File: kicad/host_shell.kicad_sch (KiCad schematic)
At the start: 242 parts, among them J1 FG PH-2AWT, J10 Memory Card Slot, J11 Conn_02x12_Odd_Even, J2 Conn_01x02, J3 Conn_01x02, J4 Conn_01x40, J5 Conn_02x10_Odd_Even, J6 Conn_01x03, J7 Conn_01x02, J8 PJ-316A-6A, J9 Conn_01x02, P1 TYPE-C16PIN, Q1 IRLML2246TRPBF, Q4 BSS138W, Q5 BSS84W, Q6 BSS138W, Q7 BSS138W, SW1 GT-TC018A-H0375-L1, SW10 Rubber, SW11 SKRPACE010_6, SW12 Rubber, SW13 Rubber, SW2 Rubber, SW3 Rubber, SW4 Rubber, SW5 Rubber, SW6 Rubber, SW7 Rubber, SW8 Rubber, SW9 Rubber, U1 MCP73831-2-OT, U10 LM4880MX/NOPB, U11 LM4890S, U12 SN74LVC1G3157DBVR, U13 SN74AHC541PWR, U14 TPS22919DCKR, U15 RV-3028-C7, U2 XC6194AA03ER-G, U3 TPS63802, U4 PCA9555PW, U5 W25Q32JVSSIQ, U6 APS6404L-3SQRx-SN, U7 RP2350B, U8 74LVC2G17GW, U9 LM4890S, Y1 ABM8-272-T3

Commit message: wip
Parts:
- removed C23: 100n, Capacitor_SMD:C_0402_1005Metric, symbol Device:C_Small
- removed JP2, JP3, JP4: SolderJumper_3_Bridged12, Jumper:SolderJumper-3_P1.3mm_Bridged12_RoundedPad1.0x1.5mm, symbol shpc_mechanical:SolderJumper_3_Bridged12
- J2, J3: footprint shpc_mechanical:SolderWirePad_1x02_SMD_150x50mil -> shpc_mechanical:SolderWirePad_1x02_SMD_2.5x1.5mm
- J7, J9: footprint shpc_mechanical:SolderWirePad_1x02_SMD_150x50mil -> shpc_mechanical:SolderWirePad_2x01_SMD_2.5x1.5mm
- SW10, SW12, SW13, SW2, SW3, SW4, SW5, SW6, SW7, SW8, SW9: footprint shpc_mechanical:Rubber_Contact -> Button_Switch_SMD:SW_SPST_PTS645Sx43SMTR92
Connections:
- net 3V3: now also U4.21 (A0)
- net GND: now also J10.10 (DET_A), U4.2 (A1), U4.3 (A2); no longer J10.9 (DET_B)
- net HSAUDIO_L: now also U8.3 (2A); no longer U8.1 (1A)
- net HSAUDIO_R: now also U8.1 (1A); no longer U8.3 (2A)
- net HSLCD_CSX: now also U7.27 (GPIO26); no longer U7.25 (GPIO24)
- net HSLCD_RDX: now also U7.25 (GPIO24); no longer U7.22 (GPIO22)
- net HSLCD_RSTX: now also U7.23 (GPIO23); no longer U7.21 (GPIO21)
- net HSLCD_WRX: now also U7.26 (GPIO25); no longer U7.23 (GPIO23)
- net HSTF_DETX: now also J10.9 (DET_B); no longer J10.10 (DET_A)
- net LCA0: no longer TP17.1
- net at R45.1: now also U7.21 (GPIO21); no longer U7.26 (GPIO25)
- net at R46.1: now also U7.22 (GPIO22); no longer U7.27 (GPIO26)
- net at U8.4 (2Y): now also R50.1; no longer R51.1
- net at U8.6 (1Y): now also R51.1; no longer R50.1
- net at U4.1 (~{INT}): now also TP17.1
- no-connect marks 17 -> 16
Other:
- moved on the sheet: C24, C25, C26, C27, C28, C29, C30, C31, C32, C33, R70

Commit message: wip
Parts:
- J11, J5: now not fitted
- SW10, SW12, SW13, SW2, SW3, SW4, SW5, SW6, SW7, SW8, SW9: value Rubber -> PTS645SL50SMTR92; now not fitted
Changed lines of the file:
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@@
 		(on_board yes)
 		(in_pos_files yes)
-		(dnp no)
+		(dnp yes)
 		(property "Reference" "SW8"
 			(at 341.122 24.638 0)
@@
 			)
 		)
-		(property "Value" "Rubber"
+		(property "Value" "PTS645SL50SMTR92"
 			(at 341.884 24.638 0)
 			(show_name no)
@@
 		(on_board yes)
 		(in_pos_files yes)
-		(dnp no)
+		(dnp yes)
 		(property "Reference" "SW10"
 			(at 341.122 28.702 0)
@@
 			)
 		)
-		(property "Value" "Rubber"
+		(property "Value" "PTS645SL50SMTR92"
 			(at 341.884 28.702 0)
 			(show_name no)
@@
 		(on_board yes)
 		(in_pos_files yes)
-		(dnp no)
+		(dnp yes)
 		(property "Reference" "SW2"
 			(at 314.452 22.606 0)
@@
 			)
 		)
-		(property "Value" "Rubber"
+		(property "Value" "PTS645SL50SMTR92"
 			(at 315.214 22.606 0)
 			(show_name no)
@@
 		(on_board yes)
 		(in_pos_files yes)
-		(dnp no)
+		(dnp yes)
 		(property "Reference" "SW3"
 			(at 314.452 24.638 0)
@@
 			)
 		)
-		(property "Value" "Rubber"
+		(property "Value" "PTS645SL50SMTR92"
 			(at 315.214 24.638 0)
 			(show_name no)
@@
 		(on_board yes)
 		(in_pos_files yes)
-		(dnp no)
+		(dnp yes)
 		(property "Reference" "SW13"
 			(at 341.376 57.15 0)
@@
 			)
 		)
-		(property "Value" "Rubber"
+		(property "Value" "PTS645SL50SMTR92"
 			(at 342.138 57.15 0)
 			(show_name no)
@@
 		(on_board yes)
 		(in_pos_files yes)
-		(dnp no)
+		(dnp yes)
 		(property "Reference" "SW12"
 			(at 341.376 55.118 0)
@@
 			)
 		)
-		(property "Value" "Rubber"
+		(property "Value" "PTS645SL50SMTR92"
 			(at 342.138 55.118 0)
 			(show_name no)
@@
 		(on_board yes)
 		(in_pos_files yes)
-		(dnp no)
+		(dnp yes)
 		(property "Reference" "SW9"
 			(at 341.122 26.67 0)
@@
 			)
 		)
-		(property "Value" "Rubber"
+		(property "Value" "PTS645SL50SMTR92"
 			(at 341.884 26.67 0)
 			(show_name no)
@@
 		(on_board yes)
 		(in_pos_files yes)
-		(dnp no)
+		(dnp yes)
 		(property "Reference" "SW5"
 			(at 314.452 28.702 0)
@@
 			)
 		)
-		(property "Value" "Rubber"
+		(property "Value" "PTS645SL50SMTR92"
 			(at 315.214 28.702 0)
 			(show_name no)
@@
 		(on_board yes)
 		(in_pos_files yes)
-		(dnp no)
+		(dnp yes)
 		(property "Reference" "SW7"
 			(at 341.122 22.606 0)
@@
 			)
 		)
-		(property "Value" "Rubber"
+		(property "Value" "PTS645SL50SMTR92"
 			(at 341.884 22.606 0)
 			(show_name no)
@@
 		(on_board yes)
 		(in_pos_files yes)
-		(dnp no)
+		(dnp yes)
 		(property "Reference" "SW6"
-			(at 331.216 81.788 90)
+			(at 329.438 82.804 90)
 			(show_name no)
 			(do_not_autoplace no)
@@
 					(size 1.27 1.27)
 				)
-				(justify left)
+				(justify right)
 			)
 		)
-		(property "Value" "Rubber"
-			(at 331.216 83.82 90)
+		(property "Value" "PTS645SL50SMTR92"
+			(at 329.438 84.836 90)
 			(show_name no)
 			(do_not_autoplace no)
@@
 					(size 1.27 1.27)
 				)
-				(justify left)
+				(justify right)
 			)
 		)
@@
 		(on_board yes)
 		(in_pos_files yes)
-		(dnp no)
+		(dnp yes)
 		(property "Reference" "SW4"
 			(at 314.452 26.67 0)
@@
 			)
 		)
-		(property "Value" "Rubber"
+		(property "Value" "PTS645SL50SMTR92"
 			(at 315.214 26.67 0)
 			(show_name no)
@@
 		(on_board yes)
 		(in_pos_files yes)
-		(dnp no)
+		(dnp yes)
 		(property "Reference" "J5"
 			(at 41.91 207.01 0)
@@
 		(on_board yes)
 		(in_pos_files yes)
-		(dnp no)
+		(dnp yes)
 		(property "Reference" "J11"
 			(at 379.73 202.438 0)

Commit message: layout review feeedback
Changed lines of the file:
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@@
 	(wire
 		(pts
-			(xy 248.92 124.46) (xy 248.92 127)
-		)
-		(stroke
-			(width 0)
-			(type default)
-		)
-	)
-	(wire
-		(pts
 			(xy 339.09 44.45) (xy 337.82 44.45)
 		)
@@
 	(wire
 		(pts
-			(xy 241.3 127) (xy 245.11 127)
+			(xy 242.57 124.46) (xy 247.65 124.46)
 		)
 		(stroke
@@
 	(wire
 		(pts
-			(xy 245.11 121.92) (xy 248.92 121.92)
+			(xy 247.65 121.92) (xy 248.92 121.92)
 		)
 		(stroke
@@
 	(wire
 		(pts
+			(xy 245.11 127) (xy 248.92 127)
+		)
+		(stroke
+			(width 0)
+			(type default)
+		)
+	)
+	(wire
+		(pts
 			(xy 127 134.62) (xy 127 133.35)
 		)
@@
 	(wire
 		(pts
+			(xy 242.57 127) (xy 241.3 127)
+		)
+		(stroke
+			(width 0)
+			(type default)
+		)
+	)
+	(wire
+		(pts
 			(xy 204.47 33.02) (xy 204.47 43.18)
 		)
@@
 	(wire
 		(pts
+			(xy 245.11 121.92) (xy 245.11 127)
+		)
+		(stroke
+			(width 0)
+			(type default)
+		)
+	)
+	(wire
+		(pts
 			(xy 58.42 40.64) (xy 48.26 40.64)
 		)
@@
 	(wire
 		(pts
-			(xy 241.3 124.46) (xy 248.92 124.46)
-		)
-		(stroke
-			(width 0)
-			(type default)
-		)
-	)
-	(wire
-		(pts
 			(xy 129.54 53.34) (xy 129.54 55.88)
 		)
@@
 	(wire
 		(pts
+			(xy 241.3 121.92) (xy 245.11 121.92)
+		)
+		(stroke
+			(width 0)
+			(type default)
+		)
+	)
+	(wire
+		(pts
 			(xy 31.75 123.19) (xy 35.56 123.19)
 		)
@@
 	(wire
 		(pts
-			(xy 241.3 121.92) (xy 241.3 124.46)
-		)
-		(stroke
-			(width 0)
-			(type default)
-		)
-	)
-	(wire
-		(pts
 			(xy 132.08 265.43) (xy 132.08 266.7)
 		)
@@
 	(wire
 		(pts
+			(xy 242.57 124.46) (xy 242.57 127)
+		)
+		(stroke
+			(width 0)
+			(type default)
+		)
+	)
+	(wire
+		(pts
 			(xy 313.69 177.8) (xy 318.77 177.8)
 		)
@@
 	(wire
 		(pts
-			(xy 245.11 127) (xy 245.11 121.92)
-		)
-		(stroke
-			(width 0)
-			(type default)
-		)
-	)
-	(wire
-		(pts
 			(xy 373.38 68.58) (xy 388.62 68.58)
 		)
@@
 	(wire
 		(pts
+			(xy 247.65 121.92) (xy 247.65 124.46)
+		)
+		(stroke
+			(width 0)
+			(type default)
+		)
+	)
+	(wire
+		(pts
 			(xy 157.48 142.24) (xy 180.34 142.24)
 		)
@@
 	)
 	(symbol
-		(lib_name "SKRPACE010_15")
+		(lib_name "SKRPACE010_4")
 		(lib_id "shpc_mechanical:SKRPACE010")
 		(at 341.63 38.1 0)
@@
 	)
 	(symbol
-		(lib_name "SKRPACE010_13")
+		(lib_name "SKRPACE010_8")
 		(lib_id "shpc_mechanical:SKRPACE010")
 		(at 341.63 48.26 0)
@@
 	)
 	(symbol
-		(lib_name "SKRPACE010_4")
+		(lib_name "SKRPACE010_3")
 		(lib_id "shpc_mechanical:SKRPACE010")
 		(at 314.96 33.02 0)
@@
 	)
 	(symbol
-		(lib_name "SKRPACE010_3")
 		(lib_id "shpc_mechanical:SKRPACE010")
 		(at 314.96 38.1 0)
@@
 	)
 	(symbol
-		(lib_name "SKRPACE010_7")
+		(lib_name "SKRPACE010_11")
 		(lib_id "shpc_mechanical:SKRPACE010")
 		(at 341.63 66.04 0)
@@
 	)
 	(symbol
-		(lib_name "SKRPACE010_5")
+		(lib_name "SKRPACE010_10")
 		(lib_id "shpc_mechanical:SKRPACE010")
 		(at 341.63 60.96 0)
@@
 	)
 	(symbol
-		(lib_name "SKRPACE010_12")
+		(lib_name "SKRPACE010_5")
 		(lib_id "shpc_mechanical:SKRPACE010")
 		(at 341.63 43.18 0)
@@
 	)
 	(symbol
-		(lib_name "SKRPACE010_14")
+		(lib_name "SKRPACE010_7")
 		(lib_id "shpc_mechanical:SKRPACE010")
 		(at 341.63 33.02 0)

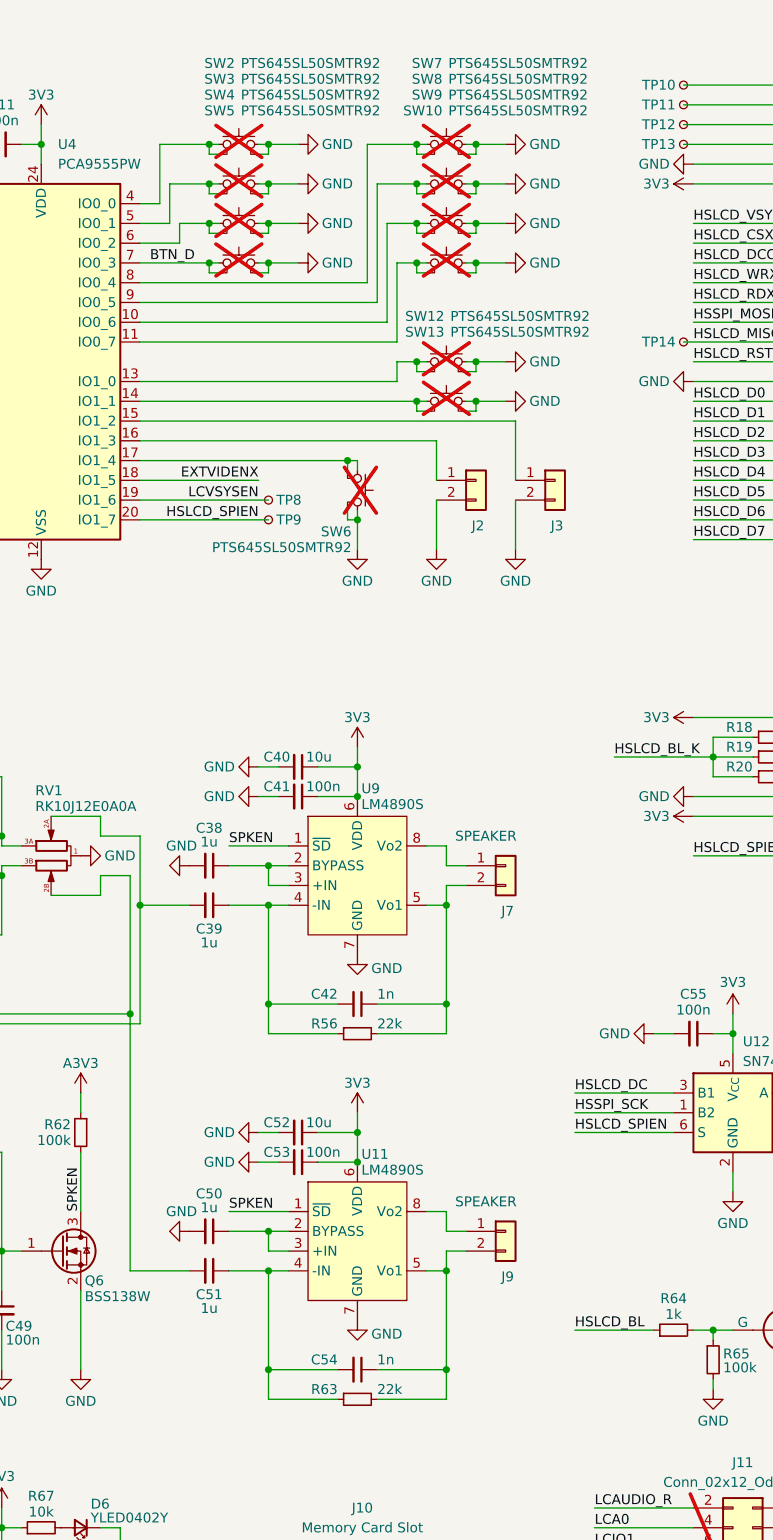
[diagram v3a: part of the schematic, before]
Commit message: fix L/R of speaker and bumper
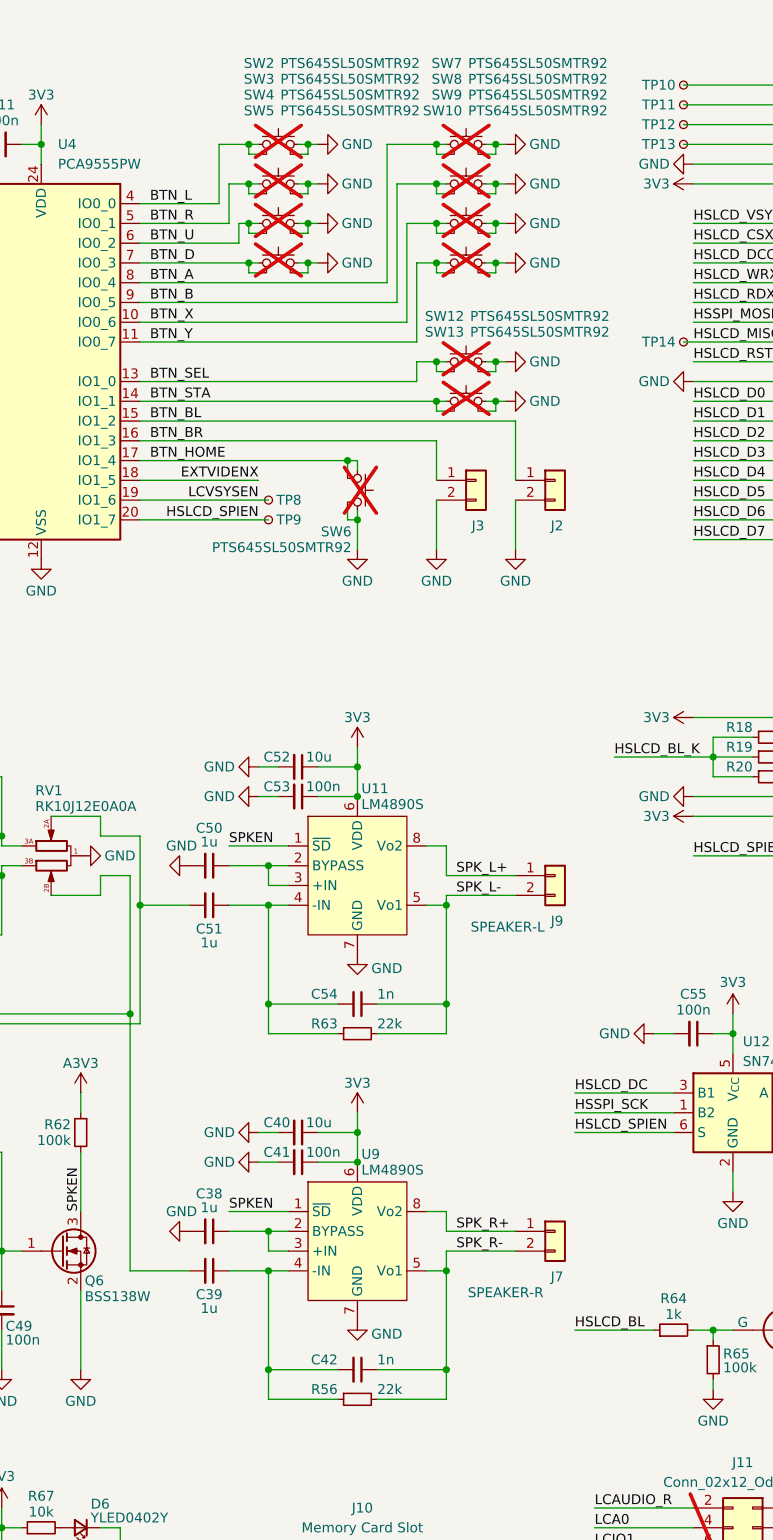
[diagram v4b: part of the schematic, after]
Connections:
- net BTN_B: now reaches SW8.1, U4.9 (IO0_5)
- net BTN_Y: now reaches SW10.1, U4.11 (IO0_7)
- net BTN_L: now reaches SW2.1, U4.4 (IO0_0)
- net at C44.2, RV1.2B: now also C39.2; no longer C51.2
- net BTN_R: now reaches SW3.1, U4.5 (IO0_1)
- net SPK_R-: now reaches C42.1, J7.2 (Pin_2), R56.2, U9.5 (Vo1)
- net BTN_STA: now reaches SW13.1, U4.14 (IO1_1)
- net BTN_BL: now reaches U4.15 (IO1_2)
- net BTN_BL: now also J2.1 (Pin_1); no longer J3.1 (Pin_1)
- net SPK_L-: now reaches C54.1, J9.2 (Pin_2), R63.2, U11.5 (Vo1)
- net SPK_L+: now reaches J9.1 (Pin_1), U11.8 (Vo2)
- net BTN_X: now reaches SW9.1, U4.10 (IO0_6)
- net BTN_SEL: now reaches SW12.1, U4.13 (IO1_0)
- net BTN_BR: now reaches U4.16 (IO1_3)
- net BTN_BR: now also J3.1 (Pin_1); no longer J2.1 (Pin_1)
- net BTN_HOME: now reaches SW6.1, U4.17 (IO1_4)
- net BTN_U: now reaches SW4.1, U4.6 (IO0_2)
- net BTN_A: now reaches SW7.1, U4.8 (IO0_4)
- net at C43.2, RV1.2A: now also C51.2; no longer C39.2
- net SPK_R+: now reaches J7.1 (Pin_1), U9.8 (Vo2)
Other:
- note added: "SPEAKER-L"
- note added: "SPEAKER-R"
- note removed: "SPEAKER"
- moved on the sheet: C38, C39, C40, C41, C42, C50, C51, C52, C53, C54, J2, J3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
